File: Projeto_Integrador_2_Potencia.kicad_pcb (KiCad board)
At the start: 2 copper layers, 149.7 x 95.2 mm, 18 parts, among them J10 Borne_CMD_Interface, J2 Vi 24V, J3 Vo 48V, J4 INA219_01x02_Socket_3.5mm, J5 INA219_01x06_Socket_2.55mm, J7 Display_01x04_Socket, J9 PWM_Connector, Q1 IRF740, Q2 47N60, U1 ESP32-DEVKIT-V1

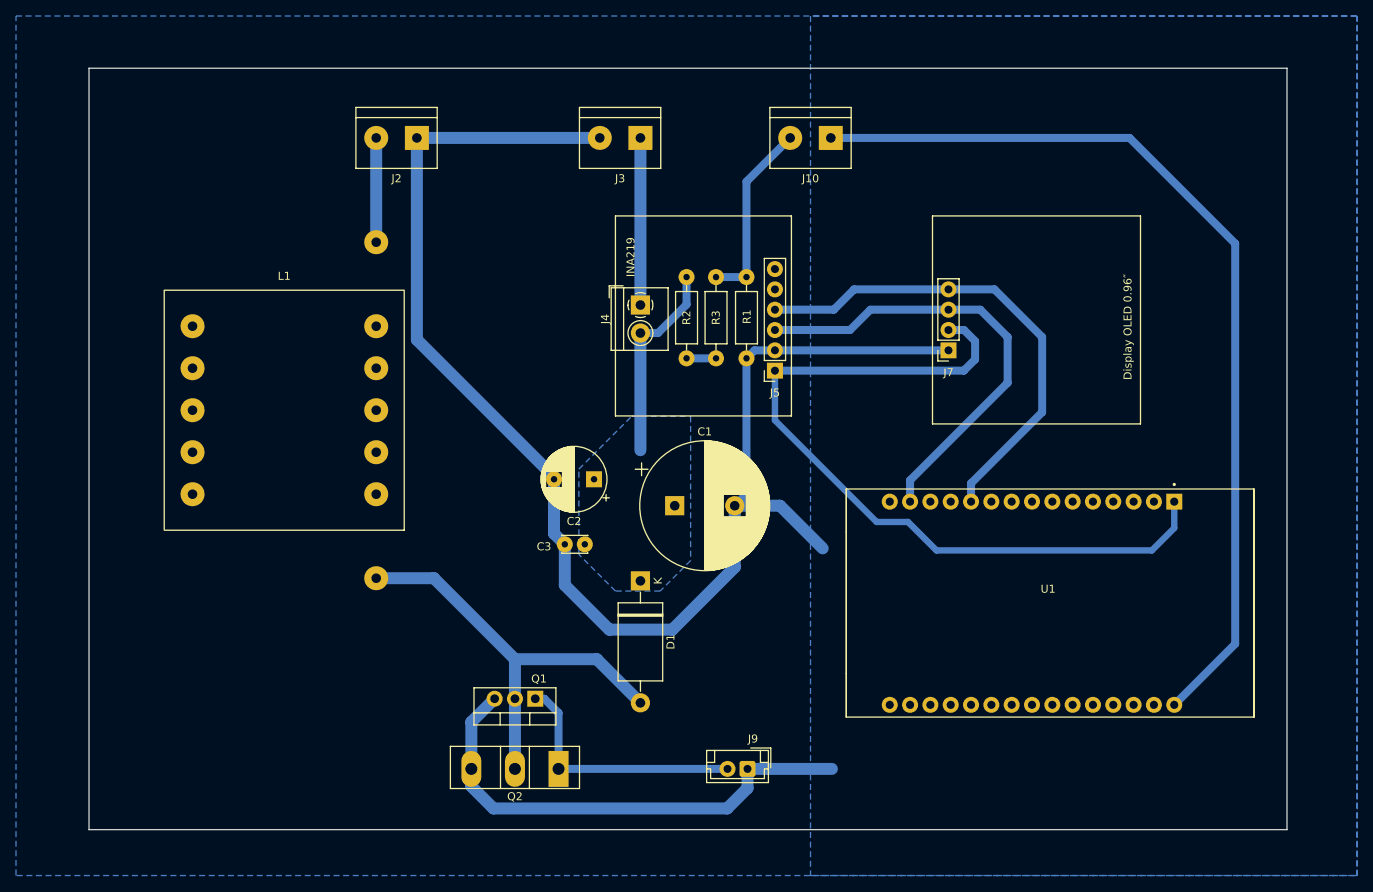
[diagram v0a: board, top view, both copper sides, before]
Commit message: Remoção das zonas de cobre
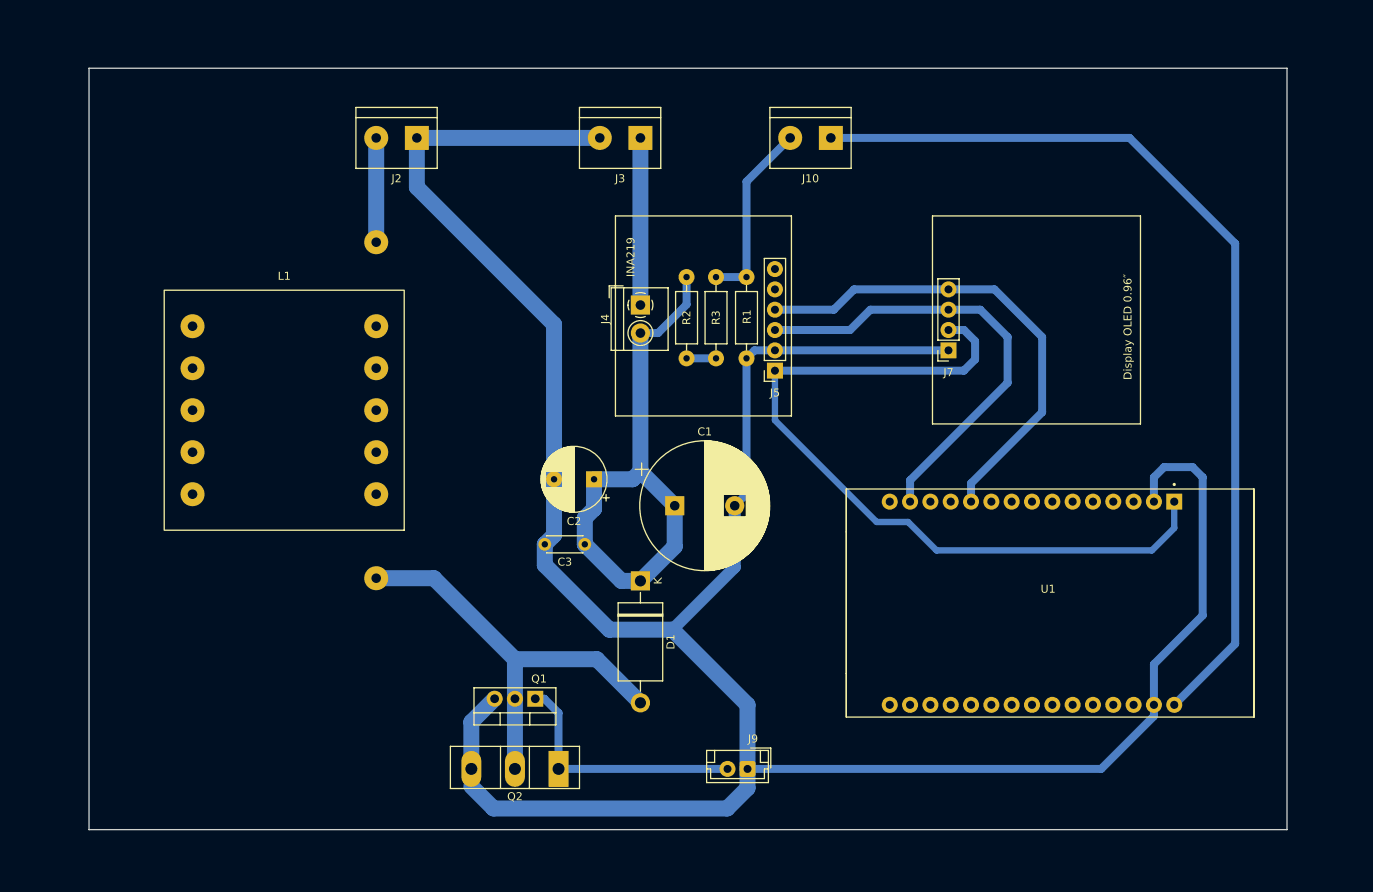
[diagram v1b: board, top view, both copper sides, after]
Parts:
- C3: footprint Capacitor_THT:C_Disc_D3.0mm_W2.0mm_P2.50mm -> Capacitor_THT:C_Disc_D4.3mm_W1.9mm_P5.00mm
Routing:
- net GND: track 240.6 -> 335.2 mm
- net INA_Vin-: track 25.3 -> 68.9 mm
- removed copper zone on B.Cu, net (none)
- removed copper zone on B.Cu, net GND
- removed copper zone on B.Cu, net INA_Vin-
